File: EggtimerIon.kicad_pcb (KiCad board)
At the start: 4 copper layers, 26 parts, among them J1 Conn_01x02, J2 Conn_01x03, J3 B2B-PH-K-S, Q1 IRLML6244, U1 ESP32-WROOM-32-N4, U2 MPU-6050, U3 MS5611-01BA, U4 CAT24C512XI-T2, U5 AP2112K-3.3

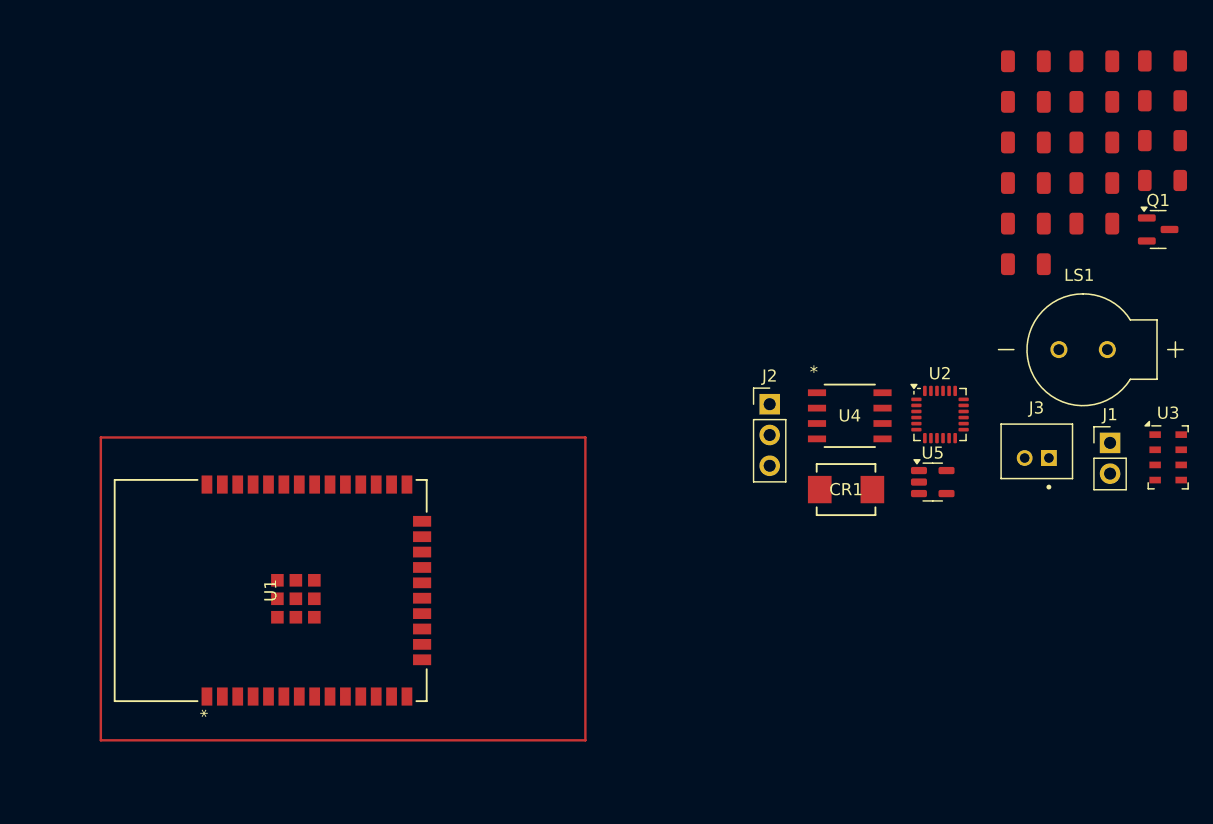
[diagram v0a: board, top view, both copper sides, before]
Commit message: Lay out almost complete
aligned parts close to their components
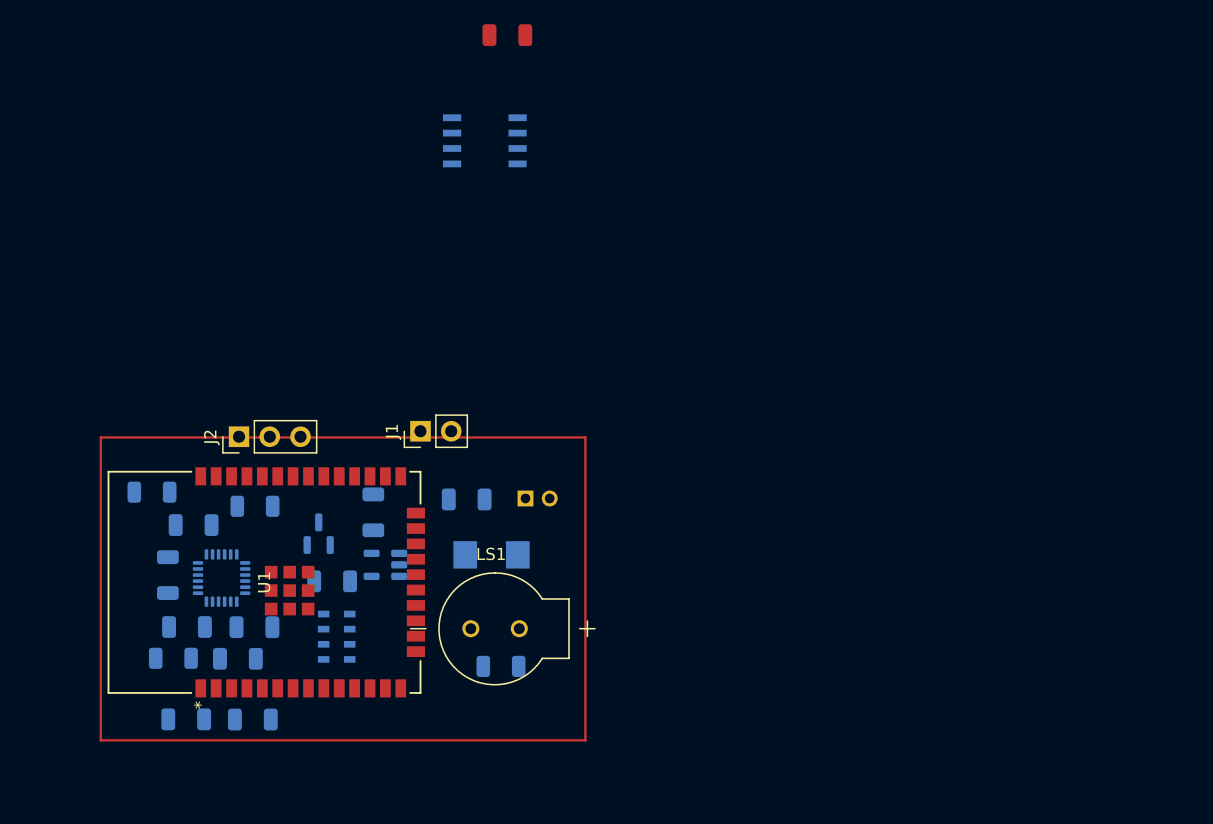
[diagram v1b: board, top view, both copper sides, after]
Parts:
- C1, C10, C11, C2, C3, C4, C5, C6, C7, C8, CR1, J3, Q1, R1, R2, R3, R4, U2, U3, U4, U5: moved to B.Cu
- moved R1 95.4 mm to (141.8, 103.6), turned to 180 degrees
- moved R2 89.5 mm to (140.0, 89.9)
- moved C7 88.3 mm to (142.9, 101.1), turned to 180 degrees
- moved C2 86.0 mm to (142.8, 108.7)
- moved C1 81.6 mm to (147.1, 103.7), turned to 180 degrees
- moved R3 80.8 mm to (148.5, 91.1), turned to 180 degrees
- moved C3 79.6 mm to (148.3, 108.7), turned to 180 degrees
- moved C5 76.5 mm to (141.3, 96.8), turned to -90 degrees
- moved C8 74.3 mm to (154.9, 97.3), turned to 180 degrees
- moved Q1 73.7 mm to (153.8, 93.4), turned to 90 degrees
- moved C4 73.5 mm to (148.5, 101.1), turned to 180 degrees
- moved C6 72.0 mm to (143.5, 92.6), turned to 180 degrees
- moved U3 70.2 mm to (155.3, 101.9), turned to 180 degrees
- moved R4 67.8 mm to (168.8, 104.3)
- moved C11 64.1 mm to (158.3, 91.6), turned to 90 degrees
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
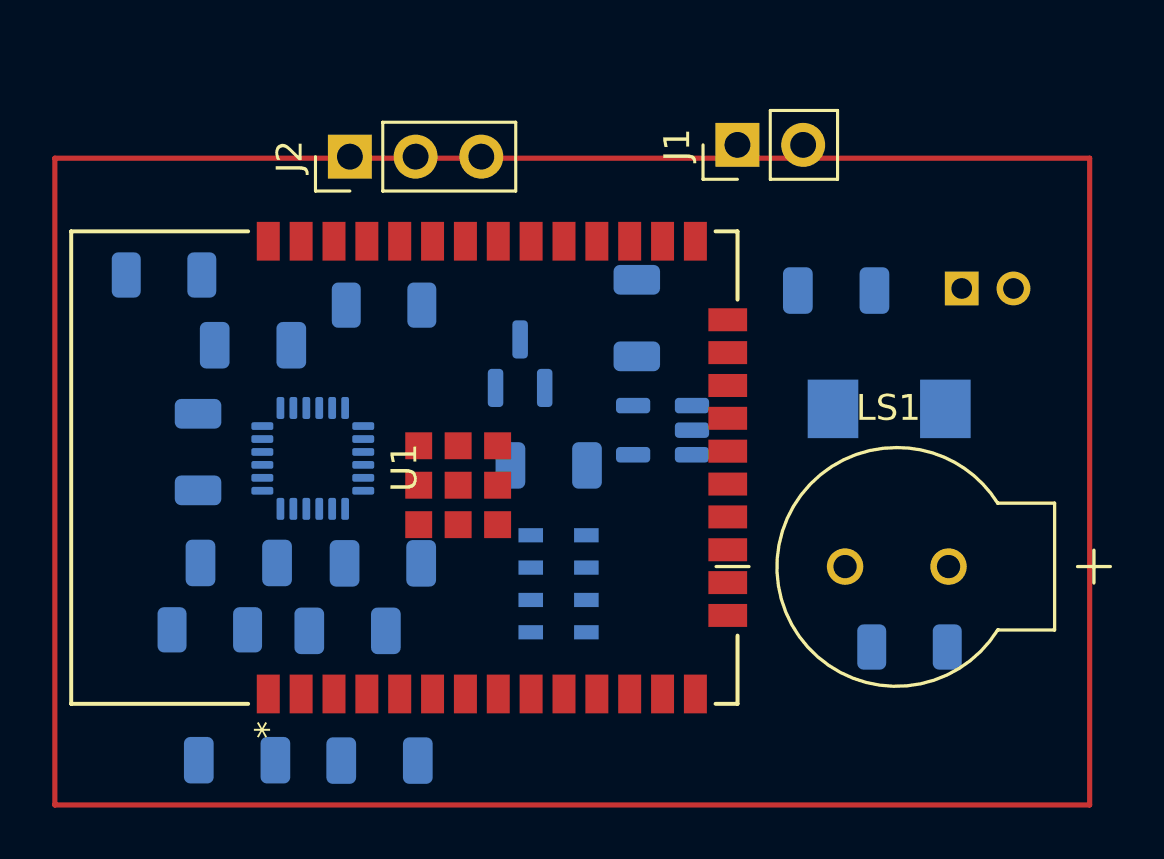
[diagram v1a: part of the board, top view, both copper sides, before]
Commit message: Finalized board settings
added ground planes
added a few 3d parts
finalized board settings
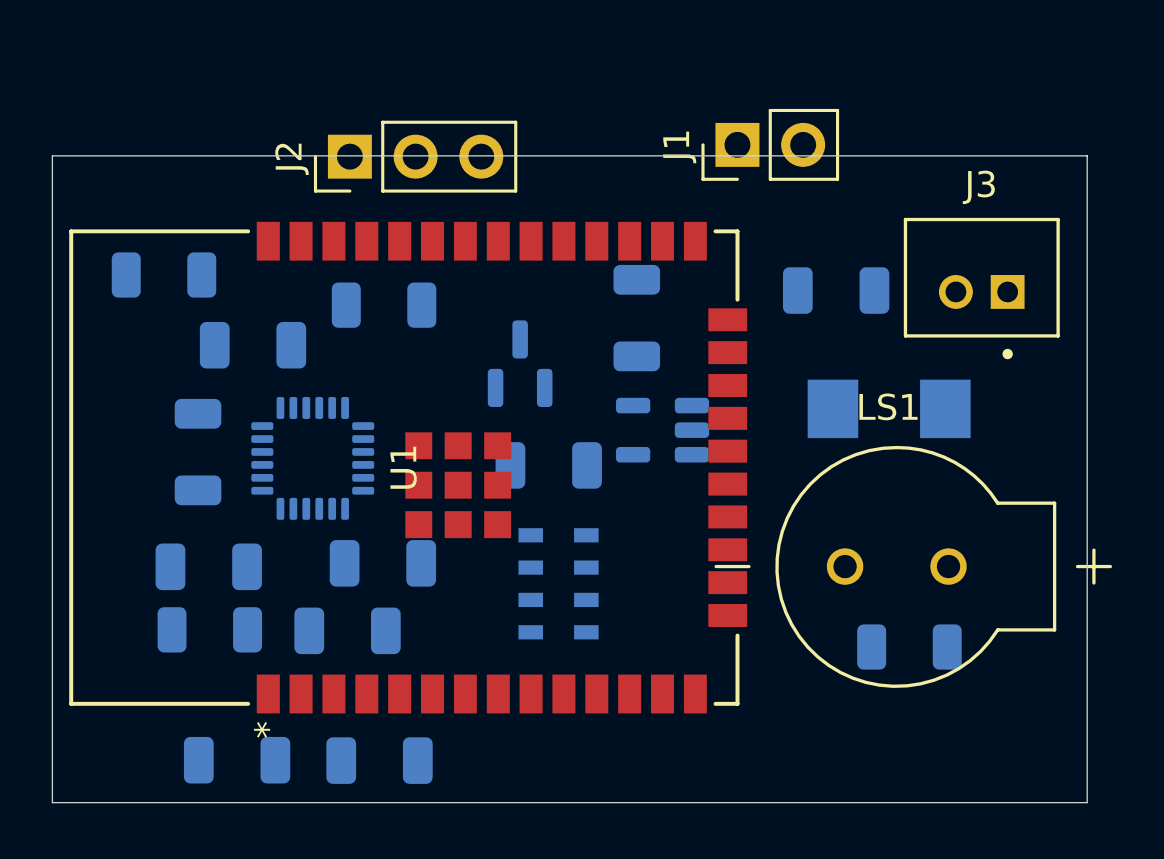
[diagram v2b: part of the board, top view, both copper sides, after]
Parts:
- J3: moved to F.Cu
- moved C7 1.17 mm to (141.8, 101.2)
- moved J3 0.26 mm to (171.6, 90.0), turned to 0 degrees
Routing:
- added copper zone on In1.Cu, net GND
- added copper zone on In2.Cu, net GND
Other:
- board outline added: 40 x 25 mm

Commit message: Completed first round of layout
Did a lot of stuff here ok?
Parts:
- added C12: 4.7uF, PCM_JLCPCB:C_1206, F.Cu at (164.2, 91.9)
- added C13: 0.1uF, PCM_JLCPCB:C_1206, F.Cu at (166.7, 91.9)
- added C14: 4.7uF, PCM_JLCPCB:C_1206, F.Cu at (169.4, 91.9)
- added C15: 0.1uF, PCM_JLCPCB:C_1206, F.Cu at (172.0, 91.9)
- added D1: SP0503BAHT, Package_TO_SOT_SMD:SOT-143, F.Cu at (176.3, 91.5)
- added J4: USB_C_Receptacle_USB2.0, Connector_USB:USB_C_Receptacle_G-Switch_GT-USB-7010ASV, F.Cu at (178.4, 98.6)
- added Q2: 2N7002, PCM_JLCPCB:Q_SOT-23, F.Cu at (158.0, 91.7)
- added Q3: 2N7002, PCM_JLCPCB:Q_SOT-23, F.Cu at (155.2, 111.5)
- added R10: 10k, PCM_JLCPCB:R_1206, F.Cu at (150.8, 87.3)
- added R11: 10k, PCM_JLCPCB:R_1206, F.Cu at (139.4, 111.0)
- added R12: 100, PCM_JLCPCB:R_1206, F.Cu at (163.4, 104.1)
- added R13: 100k, PCM_JLCPCB:R_1206, F.Cu at (162.1, 87.4)
- added R14: 100k, PCM_JLCPCB:R_1206, F.Cu at (159.0, 110.3)
- added R15: 100, PCM_JLCPCB:R_1206, F.Cu at (159.1, 105.5)
- added R5: 1k, PCM_JLCPCB:R_1206, F.Cu at (161.8, 93.0)
- added R6: 22k1, PCM_JLCPCB:R_1206, F.Cu at (165.9, 95.7)
- added R7: 47k5, PCM_JLCPCB:R_1206, F.Cu at (165.1, 108.2)
- added R8: 5k1, PCM_JLCPCB:R_1206, F.Cu at (170.9, 101.7)
- added R9: 5k1, PCM_JLCPCB:R_1206, F.Cu at (171.1, 96.0)
- added U6: CP2102N-Axx-xQFN28, Package_DFN_QFN:QFN-28-1EP_5x5mm_P0.5mm_EP3.35x3.35mm, F.Cu at (160.4, 98.8)
- U1: footprint ESP32-WROOM-32-N4:MOD_ESP32-WROOM-32_EXP -> RF_Module:ESP32-WROOM-32
- U3: moved to F.Cu
- moved Q1 23.3 mm to (166.7, 112.7)
- moved U3 12.4 mm to (147.9, 111.8), turned to 90 degrees
- moved R2 11.8 mm to (151.8, 89.0), turned to -90 degrees
- moved LS1 9.96 mm to (173.2, 109.9)
- moved J1 7.34 mm to (155.2, 87.3)
- moved J2 6.86 mm to (140.6, 87.2)
- moved U1 4.23 mm to (145.4, 99.0)
- moved J3 3.69 mm to (173.6, 86.9)
- moved U2 3.46 mm to (148.6, 95.0)
- moved C4 2.32 mm to (150.8, 101.1)
- moved C7 2.18 mm to (139.6, 101.0)
- moved C1 2.12 mm to (149.2, 104.1)
- moved C6 1.88 mm to (143.2, 94.5), turned to -90 degrees
- moved R1 1.71 mm to (140.1, 104.0), turned to 0 degrees
- moved C5 1.08 mm to (140.3, 96.5)
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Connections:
- Q1 pad 1: /IO18 -> /IO12
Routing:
- net +3V3: track 0.00 -> 54.7 mm, vias 0 -> 13
- net GND: track 0.00 -> 51.6 mm, vias 0 -> 38
- net /SDA: track 0.00 -> 48.2 mm, vias 0 -> 2
- net Net-(Q2-G): track 0.00 -> 44.8 mm, vias 0 -> 2
- net /SCL: track 0.00 -> 44.5 mm, vias 0 -> 2
- net /RXD0: track 0.00 -> 37.9 mm
- net /EN: track 0.00 -> 33.0 mm, vias 0 -> 1
- net /TXD0: track 0.00 -> 30.7 mm, vias 0 -> 2
- net VBUS: track 0.00 -> 27.5 mm
- net /USB_D+: track 0.00 -> 26.3 mm
- net /USB_D-: track 0.00 -> 21.9 mm
- net Net-(U6-VBUS): track 0.00 -> 17.0 mm, vias 0 -> 2
- net /IO12: track 0.00 -> 16.5 mm, vias 0 -> 1
- net BAT+: track 0.00 -> 15.2 mm
- net /IO0: track 0.00 -> 12.4 mm
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- added copper zone on In2.Cu, net +3V3
- removed copper zone on In2.Cu, net GND
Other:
- board size 40 x 25 mm -> 45 x 30 mm
